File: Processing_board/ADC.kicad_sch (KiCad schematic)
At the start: 58 parts, among them U10 ADS1299IPAG, U11 ADS1299IPAG

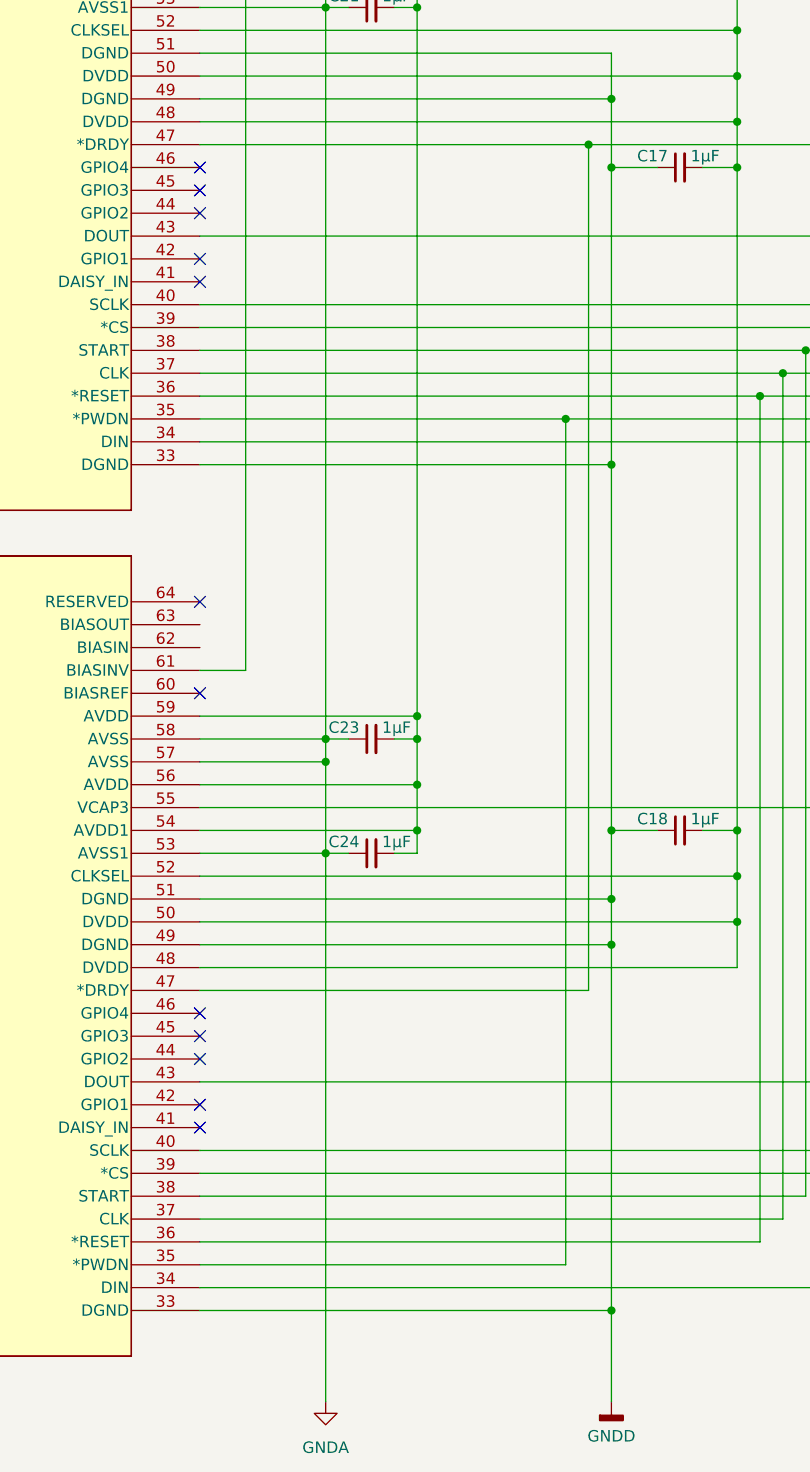
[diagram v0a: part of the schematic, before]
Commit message: fix: GPIO -> DGND
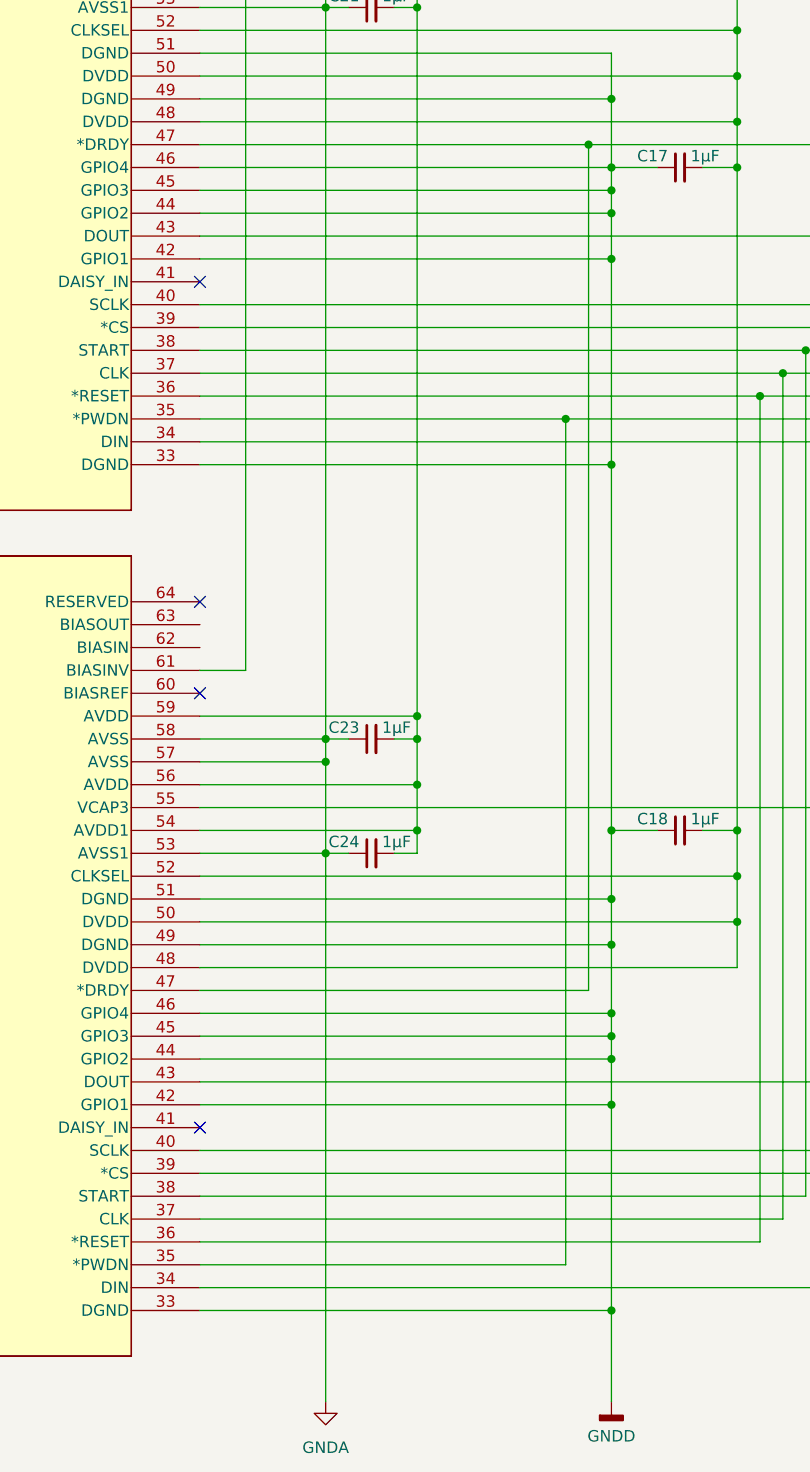
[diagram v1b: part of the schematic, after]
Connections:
- net GNDD: now also U10.42 (GPIO1), U10.44 (GPIO2), U10.45 (GPIO3), U10.46 (GPIO4), U11.42 (GPIO1), U11.44 (GPIO2), U11.45 (GPIO3), U11.46 (GPIO4)
- no-connect marks 16 -> 8
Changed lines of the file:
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@@
 	)
 	(junction
+		(at 325.12 200.66)
+		(diameter 0)
+		(color 0 0 0 0)
+	)
+	(junction
 		(at 349.25 81.28)
 		(diameter 0)
@@
 	)
 	(junction
+		(at 325.12 114.3)
+		(diameter 0)
+		(color 0 0 0 0)
+	)
+	(junction
 		(at 96.52 104.14)
 		(diameter 0)
@@
 	)
 	(junction
+		(at 325.12 106.68)
+		(diameter 0)
+		(color 0 0 0 0)
+	)
+	(junction
 		(at 341.63 129.54)
 		(diameter 0)
@@
 	)
 	(junction
+		(at 325.12 203.2)
+		(diameter 0)
+		(color 0 0 0 0)
+	)
+	(junction
 		(at 293.37 73.66)
 		(diameter 0)
@@
 	)
 	(junction
+		(at 325.12 109.22)
+		(diameter 0)
+		(color 0 0 0 0)
+	)
+	(junction
 		(at 151.13 132.08)
 		(diameter 0)
@@
 	)
 	(junction
+		(at 325.12 208.28)
+		(diameter 0)
+		(color 0 0 0 0)
+	)
+	(junction
 		(at 88.9 180.34)
 		(diameter 0)
@@
 	)
 	(junction
+		(at 325.12 198.12)
+		(diameter 0)
+		(color 0 0 0 0)
+	)
+	(junction
 		(at 111.76 104.14)
 		(diameter 0)
@@
 	)
 	(no_connect
-		(at 279.4 208.28)
-	)
-	(no_connect
-		(at 279.4 109.22)
-	)
-	(no_connect
 		(at 279.4 68.58)
 	)
@@
 	)
 	(no_connect
-		(at 279.4 106.68)
-	)
-	(no_connect
-		(at 279.4 114.3)
-	)
-	(no_connect
 		(at 208.28 195.58)
 	)
 	(no_connect
-		(at 279.4 203.2)
-	)
-	(no_connect
 		(at 279.4 210.82)
 	)
 	(no_connect
-		(at 279.4 200.66)
-	)
-	(no_connect
 		(at 208.28 101.6)
 	)
@@
 	)
 	(no_connect
-		(at 279.4 104.14)
-	)
-	(no_connect
-		(at 279.4 198.12)
-	)
-	(no_connect
 		(at 279.4 116.84)
 	)
@@
 	(wire
 		(pts
+			(xy 279.4 104.14) (xy 325.12 104.14)
+		)
+		(stroke
+			(width 0)
+			(type default)
+		)
+	)
+	(wire
+		(pts
 			(xy 323.85 72.39) (xy 323.85 71.12)
 		)
@@
 	(wire
 		(pts
-			(xy 325.12 190.5) (xy 325.12 231.14)
+			(xy 325.12 190.5) (xy 325.12 198.12)
 		)
 		(stroke
@@
 	(wire
 		(pts
+			(xy 279.4 198.12) (xy 325.12 198.12)
+		)
+		(stroke
+			(width 0)
+			(type default)
+		)
+	)
+	(wire
+		(pts
 			(xy 341.63 223.52) (xy 341.63 129.54)
 		)
@@
 	(wire
 		(pts
+			(xy 325.12 109.22) (xy 325.12 114.3)
+		)
+		(stroke
+			(width 0)
+			(type default)
+		)
+	)
+	(wire
+		(pts
 			(xy 73.66 104.14) (xy 81.28 104.14)
 		)
@@
 	(wire
 		(pts
+			(xy 325.12 200.66) (xy 325.12 203.2)
+		)
+		(stroke
+			(width 0)
+			(type default)
+		)
+	)
+	(wire
+		(pts
 			(xy 137.16 198.12) (xy 137.16 193.04)
 		)
@@
 	(wire
 		(pts
+			(xy 279.4 106.68) (xy 325.12 106.68)
+		)
+		(stroke
+			(width 0)
+			(type default)
+		)
+	)
+	(wire
+		(pts
 			(xy 300.99 73.66) (xy 303.53 73.66)
 		)
@@
 	(wire
 		(pts
+			(xy 325.12 114.3) (xy 325.12 137.16)
+		)
+		(stroke
+			(width 0)
+			(type default)
+		)
+	)
+	(wire
+		(pts
 			(xy 81.28 104.14) (xy 88.9 104.14)
 		)
@@
 	(wire
 		(pts
+			(xy 279.4 114.3) (xy 325.12 114.3)
+		)
+		(stroke
+			(width 0)
+			(type default)
+		)
+	)
+	(wire
+		(pts
 			(xy 279.4 177.8) (xy 303.53 177.8)
 		)
@@
 	(wire
 		(pts
+			(xy 325.12 208.28) (xy 325.12 231.14)
+		)
+		(stroke
+			(width 0)
+			(type default)
+		)
+	)
+	(wire
+		(pts
 			(xy 293.37 180.34) (xy 295.91 180.34)
 		)
@@
 	(wire
 		(pts
+			(xy 325.12 198.12) (xy 325.12 200.66)
+		)
+		(stroke
+			(width 0)
+			(type default)
+		)
+	)
+	(wire
+		(pts
 			(xy 208.28 119.38) (xy 137.16 119.38)
 		)
@@
 	(wire
 		(pts
+			(xy 325.12 203.2) (xy 325.12 208.28)
+		)
+		(stroke
+			(width 0)
+			(type default)
+		)
+	)
+	(wire
+		(pts
 			(xy 111.76 104.14) (xy 119.38 104.14)
 		)
@@
 	(wire
 		(pts
-			(xy 325.12 104.14) (xy 325.12 137.16)
+			(xy 325.12 104.14) (xy 325.12 106.68)
 		)
 		(stroke
@@
 	(wire
 		(pts
+			(xy 279.4 200.66) (xy 325.12 200.66)
+		)
+		(stroke
+			(width 0)
+			(type default)
+		)
+	)
+	(wire
+		(pts
 			(xy 182.88 167.64) (xy 182.88 198.12)
 		)
@@
 	(wire
 		(pts
+			(xy 325.12 106.68) (xy 325.12 109.22)
+		)
+		(stroke
+			(width 0)
+			(type default)
+		)
+	)
+	(wire
+		(pts
 			(xy 208.28 167.64) (xy 182.88 167.64)
 		)
@@
 	(wire
 		(pts
+			(xy 279.4 203.2) (xy 325.12 203.2)
+		)
+		(stroke
+			(width 0)
+			(type default)
+		)
+	)
+	(wire
+		(pts
 			(xy 151.13 121.92) (xy 151.13 127)
 		)
@@
 	(wire
 		(pts
+			(xy 279.4 109.22) (xy 325.12 109.22)
+		)
+		(stroke
+			(width 0)
+			(type default)
+		)
+	)
+	(wire
+		(pts
 			(xy 127 154.94) (xy 208.28 154.94)
 		)
@@
 		)
 		(stroke
+			(width 0)
+			(type default)
+		)
+	)
+	(wire
+		(pts
+			(xy 279.4 208.28) (xy 325.12 208.28)
+		)
+		(stroke

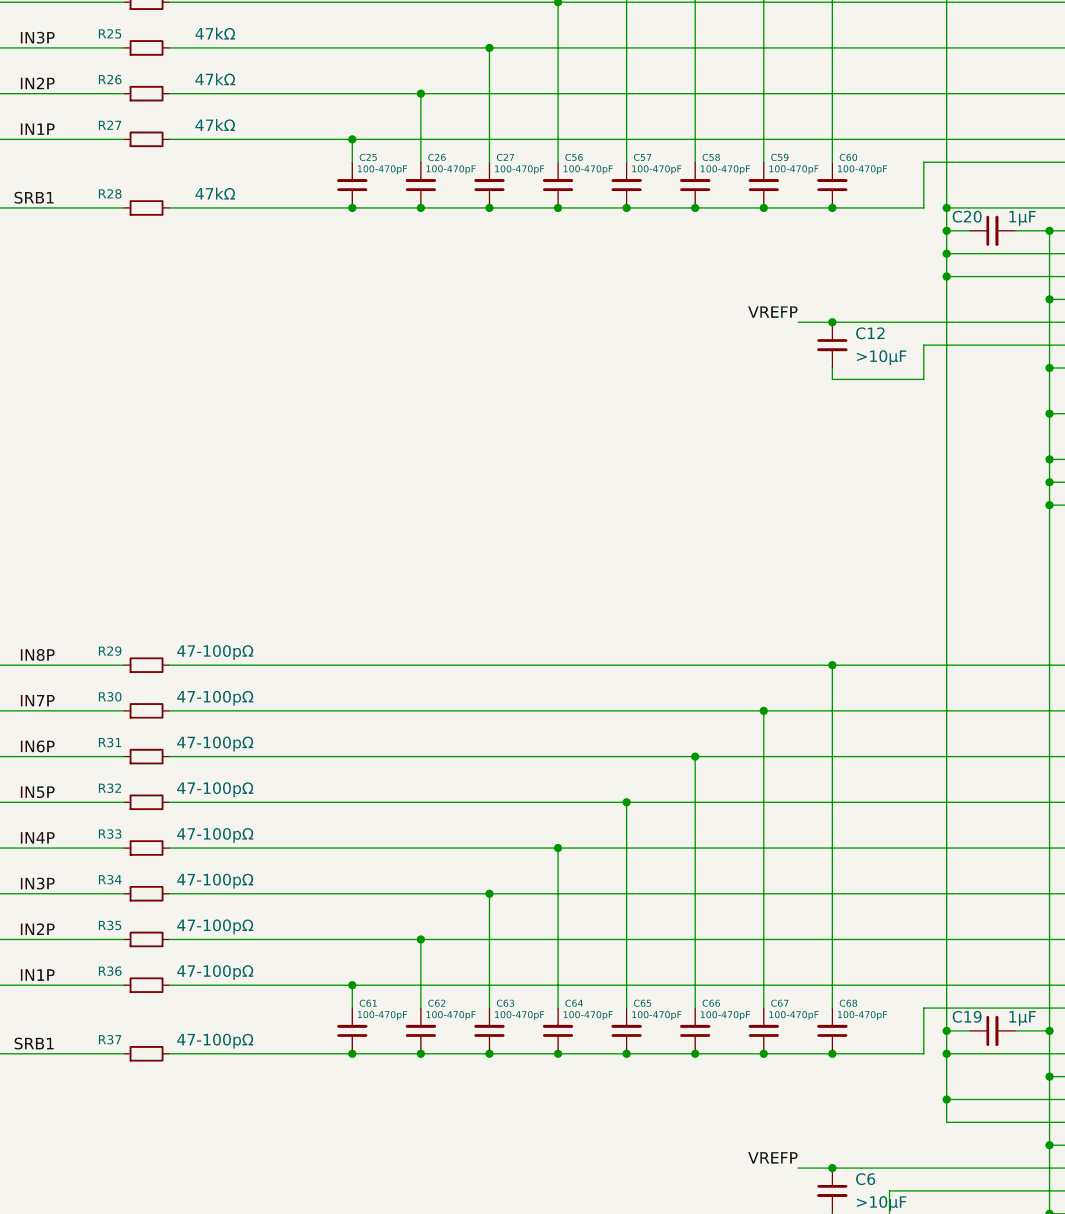
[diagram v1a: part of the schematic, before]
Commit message: fix: changed low-pass filter
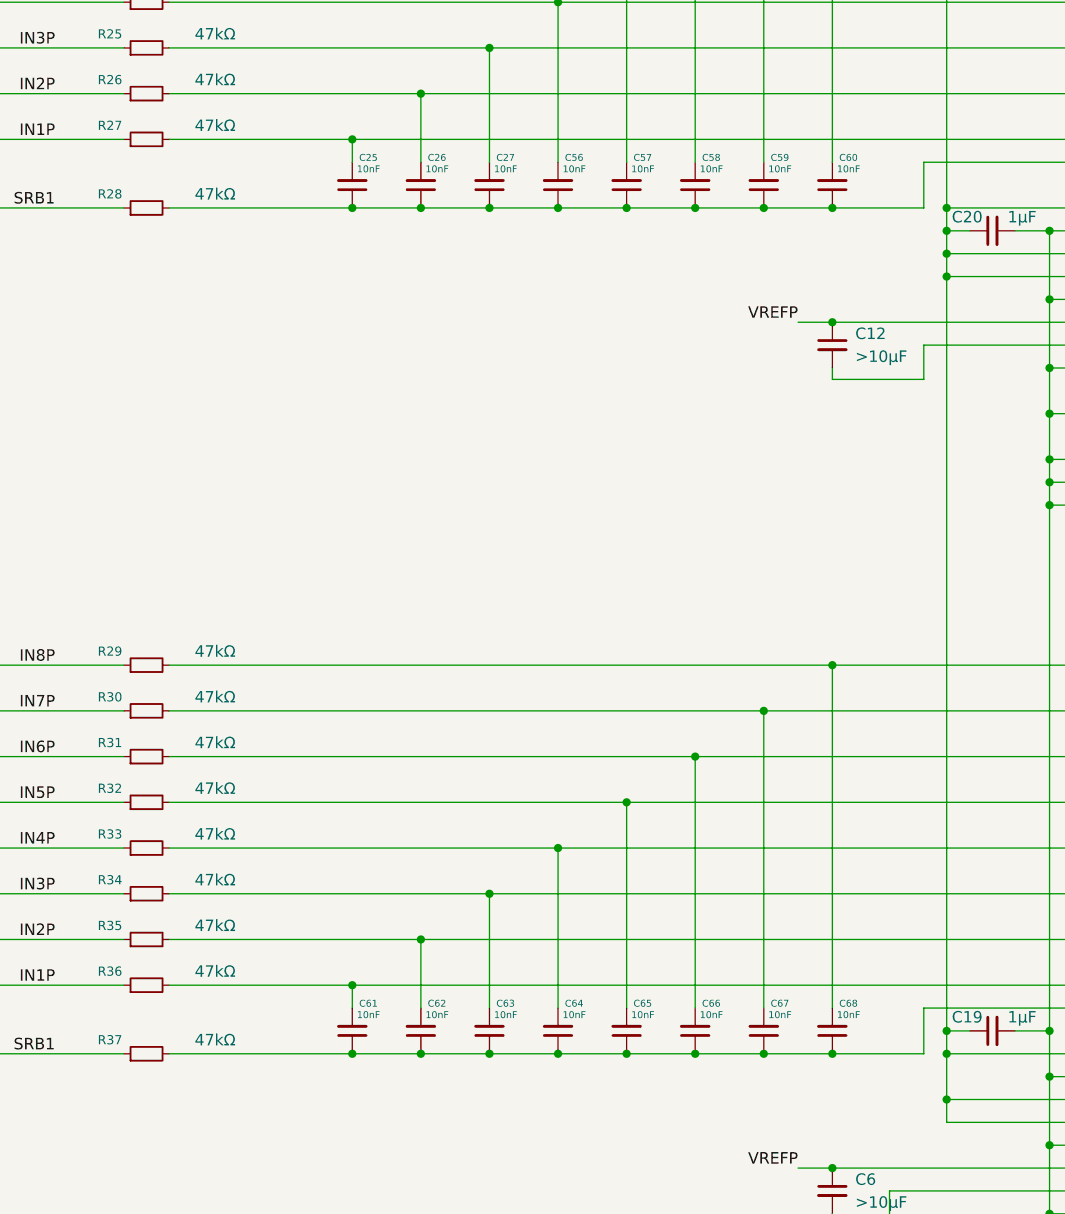
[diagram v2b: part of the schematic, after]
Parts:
- C25, C26, C27, C56, C57, C58, C59, C60, C61, C62, C63, C64, C65, C66, C67, C68: value 100-470pF -> 10nF
- R29, R30, R31, R32, R33, R34, R35, R36, R37: value 47-100pΩ -> 47kΩ
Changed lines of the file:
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@@
 			)
 		)
-		(property "Value" "100-470pF"
+		(property "Value" "10nF"
 			(at 89.408 99.822 0)
 			(effects
@@
 			)
 		)
-		(property "Value" "100-470pF"
+		(property "Value" "10nF"
 			(at 127.508 193.802 0)
 			(effects
@@
 			)
 		)
-		(property "Value" "47-100pΩ"
+		(property "Value" "47kΩ"
 			(at 58.42 168.656 90)
 			(effects
@@
 			)
 		)
-		(property "Value" "47-100pΩ"
+		(property "Value" "47kΩ"
 			(at 58.42 173.736 90)
 			(effects
@@
 			)
 		)
-		(property "Value" "100-470pF"
+		(property "Value" "10nF"
 			(at 74.168 193.802 0)
 			(effects
@@
 			)
 		)
-		(property "Value" "100-470pF"
+		(property "Value" "10nF"
 			(at 119.888 193.802 0)
 			(effects
@@
 			)
 		)
-		(property "Value" "47-100pΩ"
+		(property "Value" "47kΩ"
 			(at 58.42 163.576 90)
 			(effects
@@
 			)
 		)
-		(property "Value" "47-100pΩ"
+		(property "Value" "47kΩ"
 			(at 58.42 178.816 90)
 			(effects
@@
 			)
 		)
-		(property "Value" "100-470pF"
+		(property "Value" "10nF"
 			(at 104.648 193.802 0)
 			(effects
@@
 			)
 		)
-		(property "Value" "100-470pF"
+		(property "Value" "10nF"
 			(at 119.888 99.822 0)
 			(effects
@@
 			)
 		)
-		(property "Value" "100-470pF"
+		(property "Value" "10nF"
 			(at 104.648 99.822 0)
 			(effects
@@
 			)
 		)
-		(property "Value" "100-470pF"
+		(property "Value" "10nF"
 			(at 74.168 99.822 0)
 			(effects
@@
 			)
 		)
-		(property "Value" "100-470pF"
+		(property "Value" "10nF"
 			(at 81.788 99.822 0)
 			(effects
@@
 			)
 		)
-		(property "Value" "47-100pΩ"
+		(property "Value" "47kΩ"
 			(at 58.42 158.496 90)
 			(effects
@@
 			)
 		)
-		(property "Value" "100-470pF"
+		(property "Value" "10nF"
 			(at 97.028 193.802 0)
 			(effects
@@
 			)
 		)
-		(property "Value" "100-470pF"
+		(property "Value" "10nF"
 			(at 89.408 193.802 0)
 			(effects
@@
 			)
 		)
-		(property "Value" "100-470pF"
+		(property "Value" "10nF"
 			(at 112.268 99.822 0)
 			(effects
@@
 			)
 		)
-		(property "Value" "100-470pF"
+		(property "Value" "10nF"
 			(at 81.788 193.802 0)
 			(effects
@@
 			)
 		)
-		(property "Value" "100-470pF"
+		(property "Value" "10nF"
 			(at 112.268 193.802 0)
 			(effects
@@
 			)
 		)
-		(property "Value" "47-100pΩ"
+		(property "Value" "47kΩ"
 			(at 58.42 153.416 90)
 			(effects
@@
 			)
 		)
-		(property "Value" "47-100pΩ"
+		(property "Value" "47kΩ"
 			(at 58.42 188.976 90)
 			(effects
@@
 			)
 		)
-		(property "Value" "47-100pΩ"
+		(property "Value" "47kΩ"
 			(at 58.42 183.896 90)
 			(effects
@@
 			)
 		)
-		(property "Value" "47-100pΩ"
+		(property "Value" "47kΩ"
 			(at 58.42 196.596 90)
 			(effects
@@
 			)
 		)
-		(property "Value" "100-470pF"
+		(property "Value" "10nF"
 			(at 127.508 99.822 0)
 			(effects
@@
 			)
 		)
-		(property "Value" "100-470pF"
+		(property "Value" "10nF"
 			(at 97.028 99.822 0)
 			(effects
